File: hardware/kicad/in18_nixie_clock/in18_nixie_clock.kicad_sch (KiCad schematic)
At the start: 0 parts

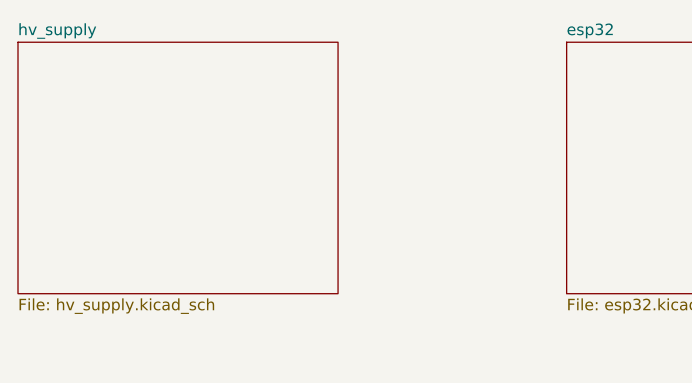
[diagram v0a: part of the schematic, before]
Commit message: Delete backups. Add HV supply schematic
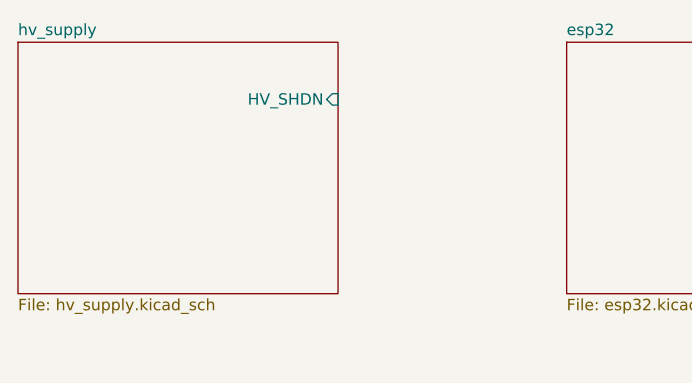
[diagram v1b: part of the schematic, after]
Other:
- sheet hv_supply ports: added HV_SHDN; removed none
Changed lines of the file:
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@@
       (effects (font (size 1.27 1.27)) (justify left top))
+    )
+    (pin "HV_SHDN" input (at 101.6 63.5 0)
+      (effects (font (size 1.27 1.27)) (justify right))
     )
   )
@@
   )
   (symbol_instances
+    (path "/cd7cdf74-a847-4330-83c0-486140a86d2d/01d0d6f5-8f06-4c83-b811-d99fb41ff0be"
+      (reference "#PWR?") (unit 1) (value "GND") (footprint "")
+    )
+    (path "/cd7cdf74-a847-4330-83c0-486140a86d2d/1bf7f6fc-60f5-4ea2-9a94-a3297ba9b92d"
+      (reference "#PWR?") (unit 1) (value "GND") (footprint "")
+    )
+    (path "/cd7cdf74-a847-4330-83c0-486140a86d2d/5923527f-aef9-46ba-bad1-a154d0d2245e"
+      (reference "#PWR?") (unit 1) (value "GND") (footprint "")
+    )
+    (path "/cd7cdf74-a847-4330-83c0-486140a86d2d/5e21889a-46fe-49c0-b699-2bd56cdb5ba9"
+      (reference "#PWR?") (unit 1) (value "GND") (footprint "")
+    )
+    (path "/cd7cdf74-a847-4330-83c0-486140a86d2d/681913dc-8a96-4ad0-8506-71ba6305cc89"
+      (reference "#PWR?") (unit 1) (value "GND") (footprint "")
+    )
+    (path "/cd7cdf74-a847-4330-83c0-486140a86d2d/6ddf7b04-6c3b-4b43-b3c7-d62cc1525fe4"
+      (reference "#PWR?") (unit 1) (value "GND") (footprint "")
+    )
+    (path "/cd7cdf74-a847-4330-83c0-486140a86d2d/8864e782-ae2b-46a1-bf06-c5852fc8962c"
+      (reference "#PWR?") (unit 1) (value "GND") (footprint "")
+    )
+    (path "/cd7cdf74-a847-4330-83c0-486140a86d2d/c863caa0-dc06-47dc-9d94-9eae56f53590"
+      (reference "#PWR?") (unit 1) (value "GND") (footprint "")
+    )
+    (path "/cd7cdf74-a847-4330-83c0-486140a86d2d/d5dfbed2-994f-415d-a249-cba9df166b86"
+      (reference "#PWR?") (unit 1) (value "GND") (footprint "")
+    )
+    (path "/cd7cdf74-a847-4330-83c0-486140a86d2d/ee25c99a-5df6-4b01-88a3-dd9cce972d52"
+      (reference "#PWR?") (unit 1) (value "GND") (footprint "")
+    )
+    (path "/cd7cdf74-a847-4330-83c0-486140a86d2d/04a4ab35-ed06-4124-8905-5758c1dbe763"
+      (reference "C?") (unit 1) (value "4.7uF, 250V") (footprint "")
+    )
+    (path "/cd7cdf74-a847-4330-83c0-486140a86d2d/1015e52d-6158-44db-b151-50a95ad56444"
+      (reference "C?") (unit 1) (value "10uF, 25V") (footprint "")
+    )
+    (path "/cd7cdf74-a847-4330-83c0-486140a86d2d/6448d495-937e-4ed9-bf10-702b4da0cf1c"
+      (reference "C?") (unit 1) (value "100nF") (footprint "Capacitor_SMD:C_0805_2012Metric_Pad1.18x1.45mm_HandSolder")
+    )
+    (path "/cd7cdf74-a847-4330-83c0-486140a86d2d/905a1a41-8aa5-4323-adc5-73429cf9384a"
+      (reference "C?") (unit 1) (value "100nF") (footprint "Capacitor_SMD:C_0805_2012Metric_Pad1.18x1.45mm_HandSolder")
+    )
+    (path "/cd7cdf74-a847-4330-83c0-486140a86d2d/b6686a91-8a0f-4ed2-bf56-d08ad3d11b17"
+      (reference "C?") (unit 1) (value "100nF, 250V") (footprint "Capacitor_SMD:C_0805_2012Metric_Pad1.18x1.45mm_HandSolder")
+    )
     (path "/cd7cdf74-a847-4330-83c0-486140a86d2d/f921dbe5-aa44-4925-b466-5e83685ffd01"
       (reference "C?") (unit 1) (value "C_Polarized") (footprint "")
     )
-    (path "/cd7cdf74-a847-4330-83c0-486140a86d2d/aa0c7971-5363-4667-8bb7-05f7ababe6ec"
-      (reference "L?") (unit 1) (value "INDUCTOR") (footprint "")
+    (path "/cd7cdf74-a847-4330-83c0-486140a86d2d/4854f649-4a19-49a5-8490-f0f4cd2de591"
+      (reference "D?") (unit 1) (value "D_Small") (footprint "")
+    )
+    (path "/cd7cdf74-a847-4330-83c0-486140a86d2d/0976c688-a0e8-4732-96ba-3c4143086723"
+      (reference "L?") (unit 1) (value "100uH") (footprint "")
+    )
+    (path "/cd7cdf74-a847-4330-83c0-486140a86d2d/027b3611-52cb-494c-8cba-e21008c315fa"
+      (reference "Q?") (unit 1) (value "IRF740") (footprint "Package_TO_SOT_THT:TO-220-3_Vertical")
+    )
+    (path "/cd7cdf74-a847-4330-83c0-486140a86d2d/0c9e7dd8-a265-4683-b749-9e9d5a9a975e"
+      (reference "R?") (unit 1) (value "1M5") (footprint "")
+    )
+    (path "/cd7cdf74-a847-4330-83c0-486140a86d2d/f4f1cad2-c6b4-4aa7-a278-a31290c480ff"
+      (reference "R?") (unit 1) (value "10K") (footprint "")
+    )
+    (path "/cd7cdf74-a847-4330-83c0-486140a86d2d/11d62b54-ace4-459e-b473-33fe4a127291"
+      (reference "RSENSE") (unit 1) (value "0.5") (footprint "")
+    )
+    (path "/cd7cdf74-a847-4330-83c0-486140a86d2d/01d47ec5-0ebf-4704-9904-39e5e290fed5"
+      (reference "RV?") (unit 1) (value "5K") (footprint "")
+    )
+    (path "/cd7cdf74-a847-4330-83c0-486140a86d2d/82d57c25-ecc1-44a8-ad7b-8d4e41db471a"
+      (reference "U?") (unit 1) (value "MAX1771CSA+") (footprint "SOIC127P600X175-8N")
     )
   )

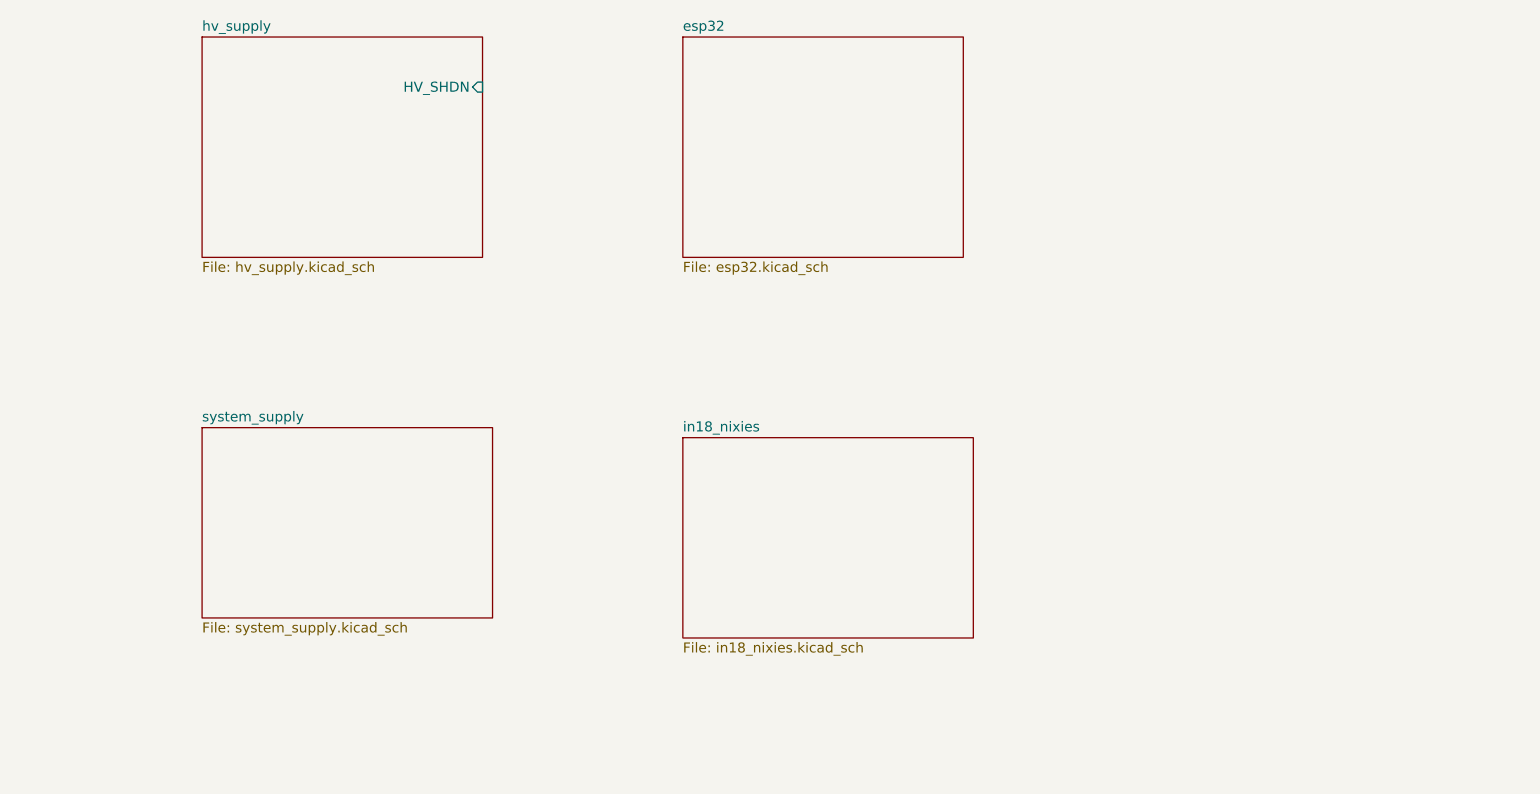
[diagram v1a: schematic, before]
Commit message: Add several schematics
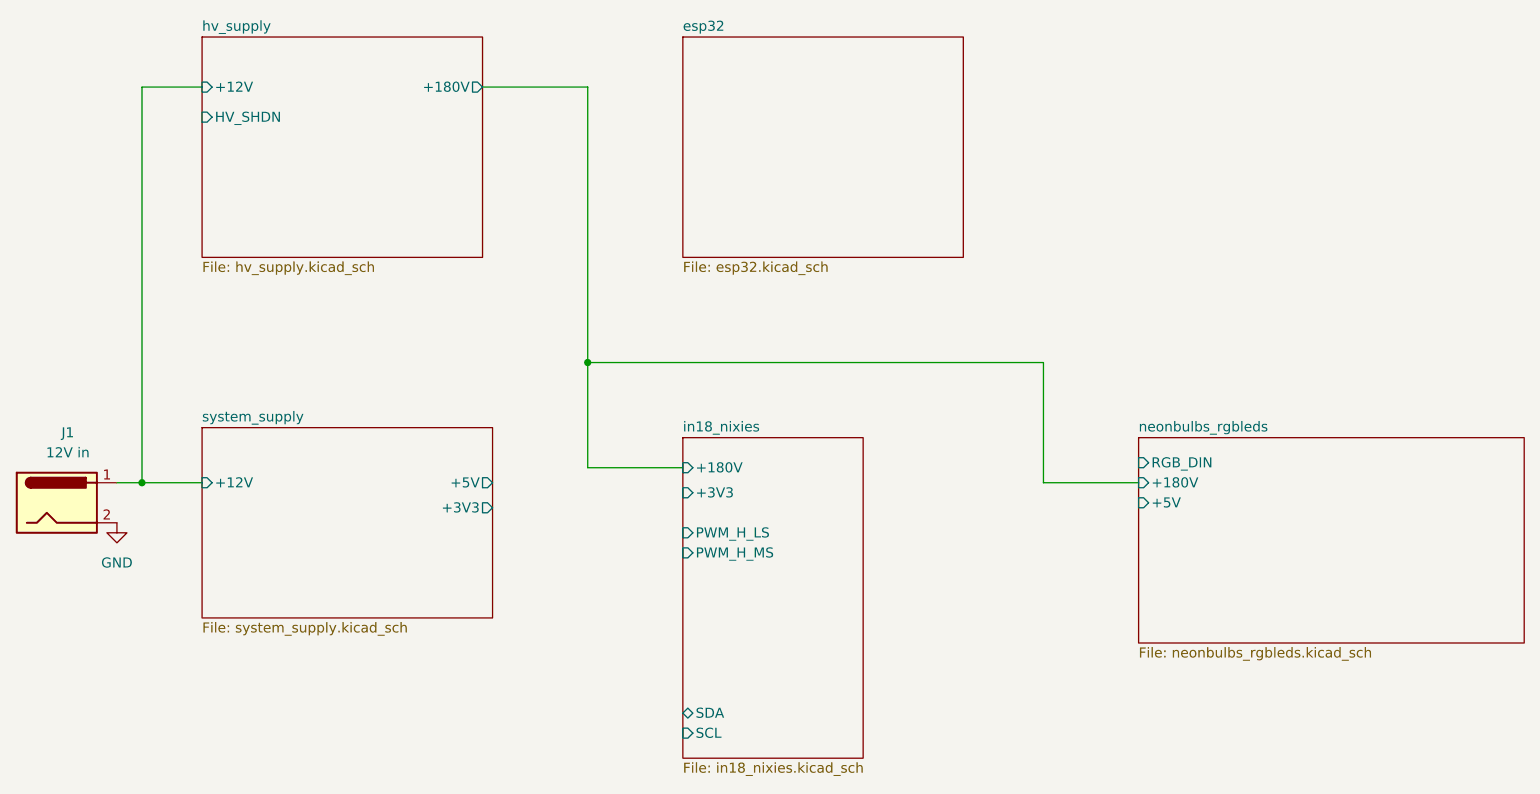
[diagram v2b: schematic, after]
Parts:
- added J1: 12V in, symbol Connector:Barrel_Jack
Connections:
- new net GND: J1.2
- new net hv_supply/+12V: J1.1
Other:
- added sheet neonbulbs_rgbleds (neonbulbs_rgbleds.kicad_sch)
- sheet hv_supply ports: added +12V, +180V; removed none
- sheet in18_nixies ports: added +180V, +3V3, PWM_H_LS, PWM_H_MS, SCL, SDA; removed none
- sheet system_supply ports: added +12V, +3V3, +5V; removed none
